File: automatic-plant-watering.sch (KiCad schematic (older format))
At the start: 52 parts, among them J1 Power, J2 USB_B_Mini, J3 MOTOR, J4 INPUT, J5 Power, Q1 BC847, Q2 BC847, Q3 TEPT4400, SW1 SW_Push, U1 ESP32-WROOM-32D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

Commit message: removing USB to UART
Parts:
- removed C3: 3.3nF, Capacitor_SMD:C_0603_1608Metric, symbol Device:C_Small
- removed C4: 22u, Capacitor_SMD:C_0603_1608Metric, symbol Device:C_Small
- removed C6: 10u, Capacitor_SMD:C_0603_1608Metric, symbol Device:C_Small
- removed C7: 0.1u, Capacitor_SMD:C_0603_1608Metric, symbol Device:C_Small
- removed F1: 3A, Fuse:Fuse_1206_3216Metric, symbol Device:Fuse
- removed J1: Power, Connector_Molex:Molex_KK-254_AE-6410-02A_1x02_P2.54mm_Vertical, symbol Connector:Conn_01x02_Male
- removed L1: 2.2u, Inductor_SMD:L_1210_3225Metric, symbol Device:L_Small
- removed R2: 100k, Resistor_SMD:R_0603_1608Metric, symbol Device:R_Small
- removed U2: TPS62132, Package_DFN_QFN:VQFN-16-1EP_3x3mm_P0.5mm_EP1.68x1.68mm_ThermalVias, symbol Regulator_Switching:TPS62132
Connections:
- wire segments 156 -> 111
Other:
- note added: "DC-DC Converter (5 to 40v - 3v3)\n"
- note removed: "DC-DC Converter (3 to 17v - 3v3)\n"

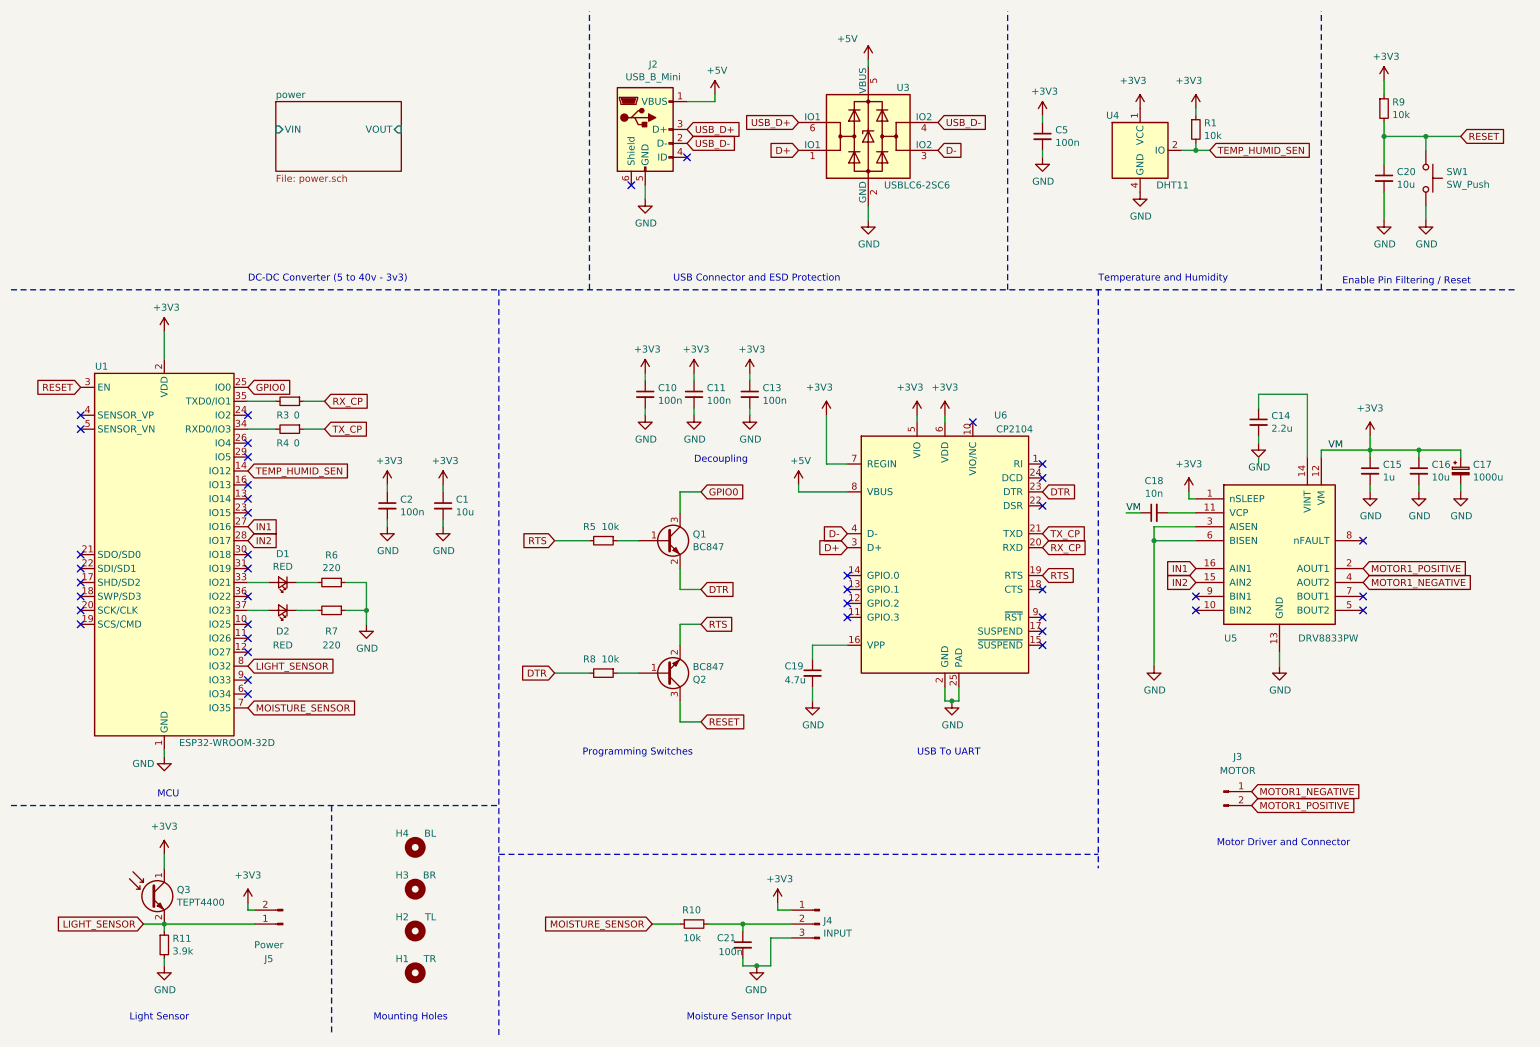
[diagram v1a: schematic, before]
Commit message: added 3d model
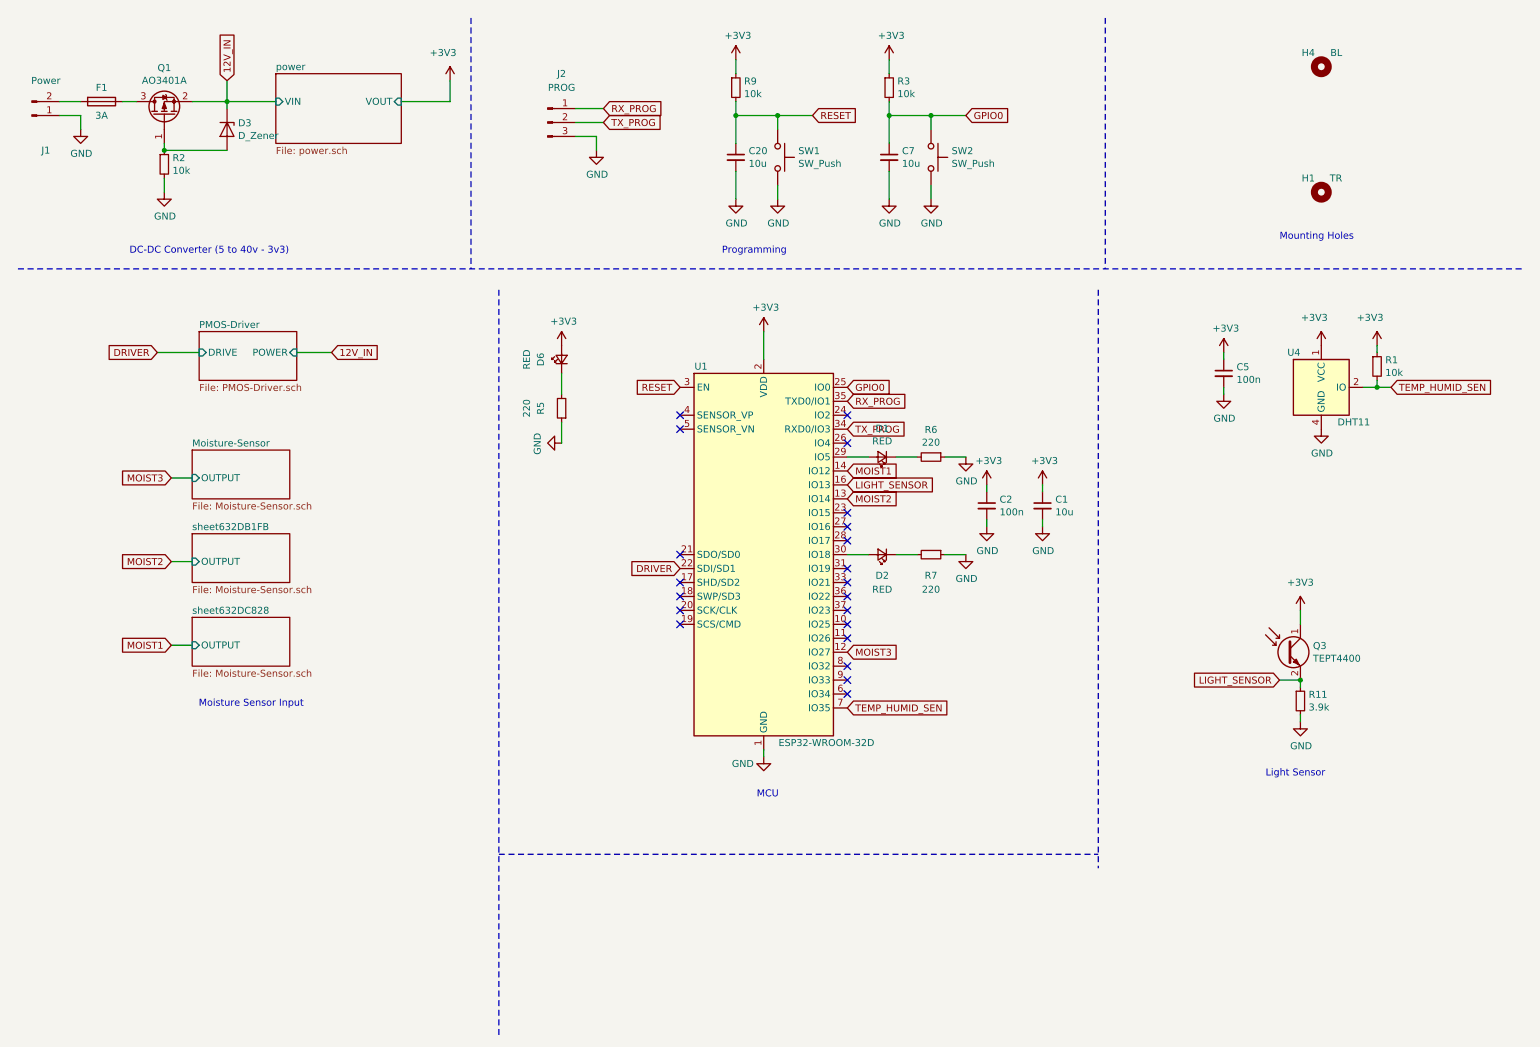
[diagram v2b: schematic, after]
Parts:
- removed C10, C11, C13, C21: 100n, Capacitor_SMD:C_0603_1608Metric, symbol Device:C_Small
- removed C14: 2.2u, Capacitor_SMD:C_0603_1608Metric, symbol Device:C_Small
- removed C15: 1u, Capacitor_SMD:C_0603_1608Metric, symbol Device:C_Small
- removed C16: 10u, Capacitor_SMD:C_0603_1608Metric, symbol Device:C_Small
- removed C17: 1000u, Capacitor_SMD:CP_Elec_10x10, symbol Device:CP_Small
- removed C18: 10n, Capacitor_SMD:C_0603_1608Metric, symbol Device:C_Small
- removed C19: 4.7u, Capacitor_SMD:C_0603_1608Metric, symbol Device:C_Small
- removed H2: TL, MountingHole:MountingHole_4.3mm_M4_Pad_Via, symbol Mechanical:MountingHole
- removed H3: BR, MountingHole:MountingHole_4.3mm_M4_Pad_Via, symbol Mechanical:MountingHole
- removed J2: USB_B_Mini, Connector_USB:USB_Mini-B_Wuerth_65100516121_Horizontal, symbol Connector:USB_B_Mini
- removed J3: MOTOR, Connector_Molex:Molex_KK-254_AE-6410-02A_1x02_P2.54mm_Vertical, symbol Connector:Conn_01x02_Male
- removed J4: INPUT, Connector_Molex:Molex_KK-254_AE-6410-03A_1x03_P2.54mm_Vertical, symbol Connector:Conn_01x03_Male
- removed J5: Power, Connector_Molex:Molex_KK-254_AE-6410-02A_1x02_P2.54mm_Vertical, symbol Connector:Conn_01x02_Male
- removed Q1, Q2: BC847, Package_TO_SOT_SMD:SOT-23, symbol Transistor_BJT:BC847
- removed R10, R8: 10k, Resistor_SMD:R_0603_1608Metric, symbol Device:R_Small
- removed R4: 0, Resistor_SMD:R_0603_1608Metric, symbol Device:R_Small
- removed U3: USBLC6-2SC6, Package_TO_SOT_SMD:SOT-23-6, symbol Power_Protection:USBLC6-2SC6
- removed U5: DRV8833PW, Package_SO:TSSOP-16_4.4x5mm_P0.65mm, symbol Driver_Motor:DRV8833PW
- removed U6: CP2104, Package_DFN_QFN:QFN-24-1EP_4x4mm_P0.5mm_EP2.6x2.6mm, symbol Interface_USB:CP2104
- added C7: 10u, Capacitor_SMD:C_0603_1608Metric, symbol Device:C_Small
- added D3: D_Zener, Diode_SMD:D_SOD-128, symbol Device:D_Zener
- added D6: RED, LED_SMD:LED_0603_1608Metric, symbol Device:LED_Small
- added F1: 3A, Fuse:Fuse_1206_3216Metric, symbol Device:Fuse
- added J1: Power, Connector_Molex:Molex_KK-254_AE-6410-02A_1x02_P2.54mm_Vertical, symbol Connector:Conn_01x02_Male
- added J2: PROG, Connector_PinHeader_2.54mm:PinHeader_1x03_P2.54mm_Vertical, symbol Connector:Conn_01x03_Male
- added Q1: AO3401A, Package_TO_SOT_SMD:SOT-23, symbol Transistor_FET:AO3401A
- added R2: 10k, Resistor_SMD:R_0603_1608Metric, symbol Device:R_Small
- added SW2: SW_Push, Button_Switch_SMD:SW_Push_1P1T_NO_6x6mm_H9.5mm, symbol Switch:SW_Push
- C1, C20: LCSC PART # (none) -> C96446
- C2, C5: LCSC PART # (none) -> C30926
- D1, D2: LCSC PART # (none) -> C2286
- H1, H4: footprint MountingHole:MountingHole_4.3mm_M4_Pad_Via -> MountingHole:MountingHole_2.2mm_M2_DIN965
- R1, R9: LCSC PART # (none) -> C25197
- R11: LCSC PART # (none) -> C23018
- R3: value 0 -> 10k; LCSC PART # (none) -> C25197
- R5: value 10k -> 220; LCSC PART # (none) -> C4190
- R6, R7: LCSC PART # (none) -> C4190
- SW1: LCSC PART # (none) -> C843627
- U1: LCSC PART # (none) -> C82899
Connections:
- net MOISTURE_SENSOR is gone; now on net TEMP_HUMID_SEN: U1.7 (IO35)
- net RX_CP is gone; now on net +3V3: R3.1
- net +3V3: now also D6.2 (A)
- net GND: now also R5.1, C7.2, J1.1 (Pin_1), J2.3 (Pin_3), R2.2, SW2.2
- net GPIO0: now also R3.2, C7.1, SW2.1
- net LIGHT_SENSOR: now also U1.16 (IO13); no longer U1.8 (IO32)
- net TEMP_HUMID_SEN: no longer U1.14 (IO12)
- net MOIST3: now reaches U1.12 (IO27)
- net MOIST2: now reaches U1.13 (IO14)
- net DRIVER: now reaches U1.22 (SDI/SD1)
- net at U1.29 (IO5): now also D1.2 (A)
- net at U1.30 (IO18): now also D2.2 (A)
- net at U1.33 (IO21): no longer D1.2 (A)
- net TX_PROG: now reaches U1.34 (RXD0/IO3)
- net TX_PROG: now also J2.2 (Pin_2)
- net RX_PROG: now reaches U1.35 (TXD0/IO1)
- net RX_PROG: now also J2.1 (Pin_1); no longer R3.2
- net at U1.37 (IO23): no longer D2.2 (A)
- net IN1: no longer names the net of U1.27 (IO16)
- net IN2: no longer names the net of U1.28 (IO17)
- net RTS: no longer names the net of R5.2
- net RTS: now also D6.1 (K)
- new net: F1.2, J1.2 (Pin_2)
- new net: F1.1, Q1.3 (D)
- new net: D3.2 (A), Q1.1 (G), R2.1
- new net 12V_IN: D3.1 (K), Q1.2 (S)
- new net MOIST1: U1.14 (IO12)
- no-connect marks 41 -> 21
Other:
- note added: "Programming"
- note removed: "Decoupling\n"
- note removed: "Enable Pin Filtering / Reset\n\n"
- note removed: "Motor Driver and Connector"
- note removed: "Programming Switches\n"
- note removed: "Temperature and Humidity\n"
- note removed: "USB Connector and ESD Protection\n"
- note removed: "USB To UART\n"
- moved on the sheet: C1, C2, C20, C5, D1, D2, H1, H4, Q3, R1, R11, R6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

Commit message: fixed up some mistakes
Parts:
- C1, C20, C7: LCSC (none) -> C96446
- C2, C5: LCSC (none) -> C30926
- D1, D2, D6: LCSC (none) -> C2286
- D3: LCSC (none) -> C253489
- F1: LCSC (none) -> C207036
- Q1: LCSC (none) -> C2997136
- R1, R2, R3, R9: LCSC (none) -> C25197
- R11: LCSC (none) -> C23018
- R5, R6, R7: LCSC (none) -> C4190
- SW1, SW2: LCSC (none) -> C843627
- U1: LCSC (none) -> C82899
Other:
- moved on the sheet: D6
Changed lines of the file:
@@
 F 3 "https://www.espressif.com/sites/default/files/documentation/esp32-wroom-32d_esp32-wroom-32u_datasheet_en.pdf" H 5550 4400 50  0001 C CNN
 F 4 "C82899" H 5850 4350 50  0001 C CNN "LCSC PART #"
+F 5 "C82899" H 5850 4350 50  0001 C CNN "LCSC"
 	1    5850 4350
 	1    0    0    -1
@@
 F 3 "~" H 5650 1000 50  0001 C CNN
 F 4 "C25197" H 5650 1000 50  0001 C CNN "LCSC PART #"
+F 5 "C25197" H 5650 1000 50  0001 C CNN "LCSC"
 	1    5650 1000
 	1    0    0    -1
@@
 F 3 "~" H 5650 1500 50  0001 C CNN
 F 4 "C96446" H 5650 1500 50  0001 C CNN "LCSC PART #"
+F 5 "C96446" H 5650 1500 50  0001 C CNN "LCSC"
 	1    5650 1500
 	1    0    0    -1
@@
 F 3 "~" H 5950 1700 50  0001 C CNN
 F 4 "C843627" H 5950 1500 50  0001 C CNN "LCSC PART #"
+F 5 "C843627" H 5950 1500 50  0001 C CNN "LCSC"
 	1    5950 1500
 	0    1    1    0
@@
 F 3 "~" V 6700 3650 50  0001 C CNN
 F 4 "C2286" H 6700 3650 50  0001 C CNN "LCSC PART #"
+F 5 "C2286" H 6700 3650 50  0001 C CNN "LCSC"
 	1    6700 3650
 	-1   0    0    1
@@
 F 3 "~" V 6700 4350 50  0001 C CNN
 F 4 "C2286" H 6700 4350 50  0001 C CNN "LCSC PART #"
+F 5 "C2286" H 6700 4350 50  0001 C CNN "LCSC"
 	1    6700 4350
 	-1   0    0    1
@@
 F 3 "~" H 7050 3650 50  0001 C CNN
 F 4 "C4190" H 7050 3650 50  0001 C CNN "LCSC PART #"
+F 5 "C4190" H 7050 3650 50  0001 C CNN "LCSC"
 	1    7050 3650
 	0    1    1    0
@@
 F 3 "~" H 7050 4350 50  0001 C CNN
 F 4 "C4190" H 7050 4350 50  0001 C CNN "LCSC PART #"
+F 5 "C4190" H 7050 4350 50  0001 C CNN "LCSC"
 	1    7050 4350
 	0    1    1    0
@@
 F 3 "~" H 9150 3050 50  0001 C CNN
 F 4 "C30926" H 9150 3050 50  0001 C CNN "LCSC PART #"
+F 5 "C30926" H 9150 3050 50  0001 C CNN "LCSC"
 	1    9150 3050
 	1    0    0    -1
@@
 F 3 "~" H 10250 3000 50  0001 C CNN
 F 4 "C25197" H 10250 3000 50  0001 C CNN "LCSC PART #"
+F 5 "C25197" H 10250 3000 50  0001 C CNN "LCSC"
 	1    10250 3000
 	1    0    0    -1
@@
 F 3 "~" H 7450 4000 50  0001 C CNN
 F 4 "C30926" H 7450 4000 50  0001 C CNN "LCSC PART #"
+F 5 "C30926" H 7450 4000 50  0001 C CNN "LCSC"
 	1    7450 4000
 	1    0    0    -1
@@
 F 3 "~" H 9700 5400 50  0001 C CNN
 F 4 "C23018" H 9700 5400 50  0001 C CNN "LCSC PART #"
+F 5 "C23018" H 9700 5400 50  0001 C CNN "LCSC"
 	1    9700 5400
 	1    0    0    -1
@@
 F 3 "~" H 7850 4000 50  0001 C CNN
 F 4 "C96446" H 7850 4000 50  0001 C CNN "LCSC PART #"
+F 5 "C96446" H 7850 4000 50  0001 C CNN "LCSC"
 	1    7850 4000
 	1    0    0    -1
@@
 F 3 "~" H 6750 1000 50  0001 C CNN
 F 4 "C25197" H 6750 1000 50  0001 C CNN "LCSC PART #"
+F 5 "C25197" H 6750 1000 50  0001 C CNN "LCSC"
 	1    6750 1000
 	1    0    0    -1
@@
 F 3 "~" H 6750 1500 50  0001 C CNN
 F 4 "C96446" H 6750 1500 50  0001 C CNN "LCSC PART #"
+F 5 "C96446" H 6750 1500 50  0001 C CNN "LCSC"
 	1    6750 1500
 	1    0    0    -1
@@
 F 3 "~" H 7050 1700 50  0001 C CNN
 F 4 "C843627" H 7050 1500 50  0001 C CNN "LCSC PART #"
+F 5 "C843627" H 7050 1500 50  0001 C CNN "LCSC"
 	1    7050 1500
 	0    1    1    0
@@
 F 3 "~" H 1100 1100 50  0001 C CNN
 F 4 "C207036" H 1100 1100 50  0001 C CNN "LCSC PART #"
+F 5 "C207036" H 1100 1100 50  0001 C CNN "LCSC"
 	1    1100 1100
 	0    1    1    0
@@
 F 3 "http://www.aosmd.com/pdfs/datasheet/AO3401A.pdf" H 1550 1200 50  0001 L CNN
 F 4 "C2997136" H 1550 1200 50  0001 C CNN "LCSC PART #"
+F 5 "C2997136" H 1550 1200 50  0001 C CNN "LCSC"
 	1    1550 1200
 	0    -1   -1   0
@@
 F 3 "~" H 1550 1550 50  0001 C CNN
 F 4 "C25197" H 1550 1550 50  0001 C CNN "LCSC PART #"
+F 5 "C25197" H 1550 1550 50  0001 C CNN "LCSC"
 	1    1550 1550
 	1    0    0    -1
@@
 F 3 "~" H 2000 1300 50  0001 C CNN
 F 4 "C253489" H 2000 1300 50  0001 C CNN "LCSC PART #"
+F 5 "C253489" H 2000 1300 50  0001 C CNN "LCSC"
 	1    2000 1300
 	0    1    1    0
@@
 L Device:LED_Small D6
 U 1 1 63434BB3
-P 4400 2950
-F 0 "D6" H 4400 3100 50  0000 C CNN
-F 1 "RED" H 4400 3200 50  0000 C CNN
-F 2 "LED_SMD:LED_0603_1608Metric" V 4400 2950 50  0001 C CNN
-F 3 "~" V 4400 2950 50  0001 C CNN
-F 4 "C2286" H 4400 2950 50  0001 C CNN "LCSC PART #"
-	1    4400 2950
+P 4400 3050
+F 0 "D6" H 4400 3200 50  0000 C CNN
+F 1 "RED" H 4400 3300 50  0000 C CNN
+F 2 "LED_SMD:LED_0603_1608Metric" V 4400 3050 50  0001 C CNN
+F 3 "~" V 4400 3050 50  0001 C CNN
+F 4 "C2286" H 4400 3050 50  0001 C CNN "LCSC PART #"
+F 5 "C2286" H 4400 3050 50  0001 C CNN "LCSC"
+	1    4400 3050
 	0    -1   -1   0
 $EndComp
@@
 F 3 "~" H 4400 3300 50  0001 C CNN
 F 4 "C4190" H 4400 3300 50  0001 C CNN "LCSC PART #"
+F 5 "C4190" H 4400 3300 50  0001 C CNN "LCSC"
 	1    4400 3300
 	-1   0    0    1
@@
 $EndComp
 Wire Wire Line
-	4400 3050 4400 3200
-Wire Wire Line
 	4400 3400 4400 3550
 $Comp
@@
 	1    0    0    -1
 $EndComp
+Wire Wire Line
+	4400 3150 4400 3200
+Wire Wire Line
+	4400 2850 4400 2950
 $EndSCHEMATC
